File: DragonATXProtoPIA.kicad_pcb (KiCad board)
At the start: 2 copper layers, 168.7 x 104.9 mm, 78 parts, among them IC1 MC6821, IC10 MT8816, IC11 74LS138, IC12 W65C51, IC13 MAX232, IC14 M48Tx2, IC15 74LS21, IC2 MC6821, IC3 74LS138, IC4 4050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

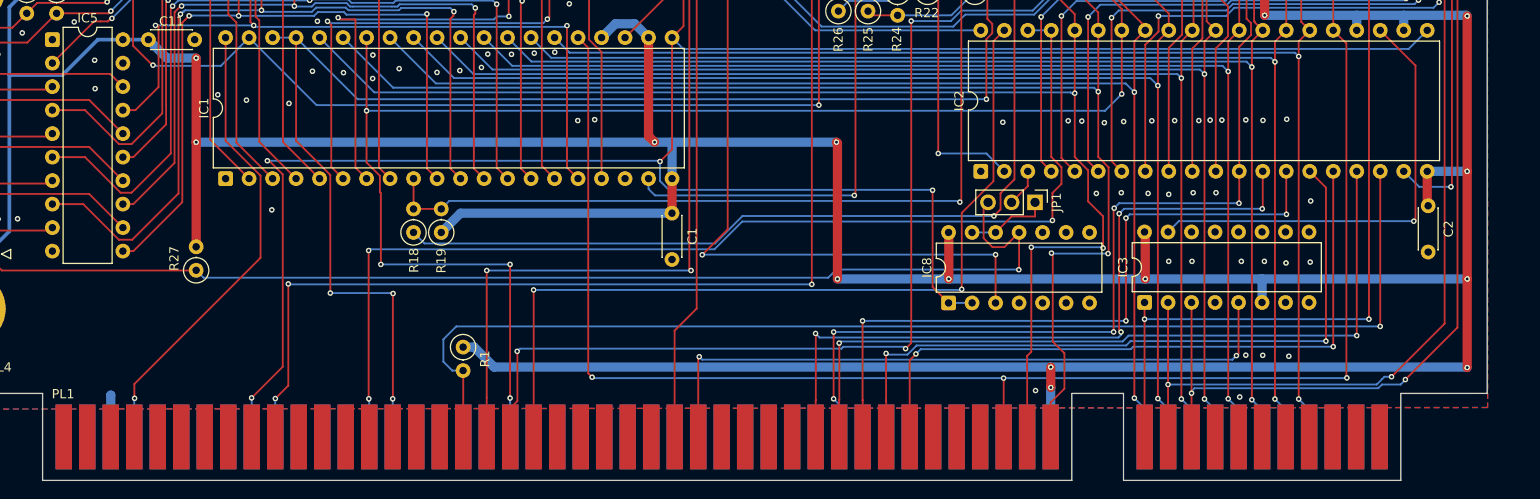
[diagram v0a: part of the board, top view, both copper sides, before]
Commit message: upgrade card edge spec
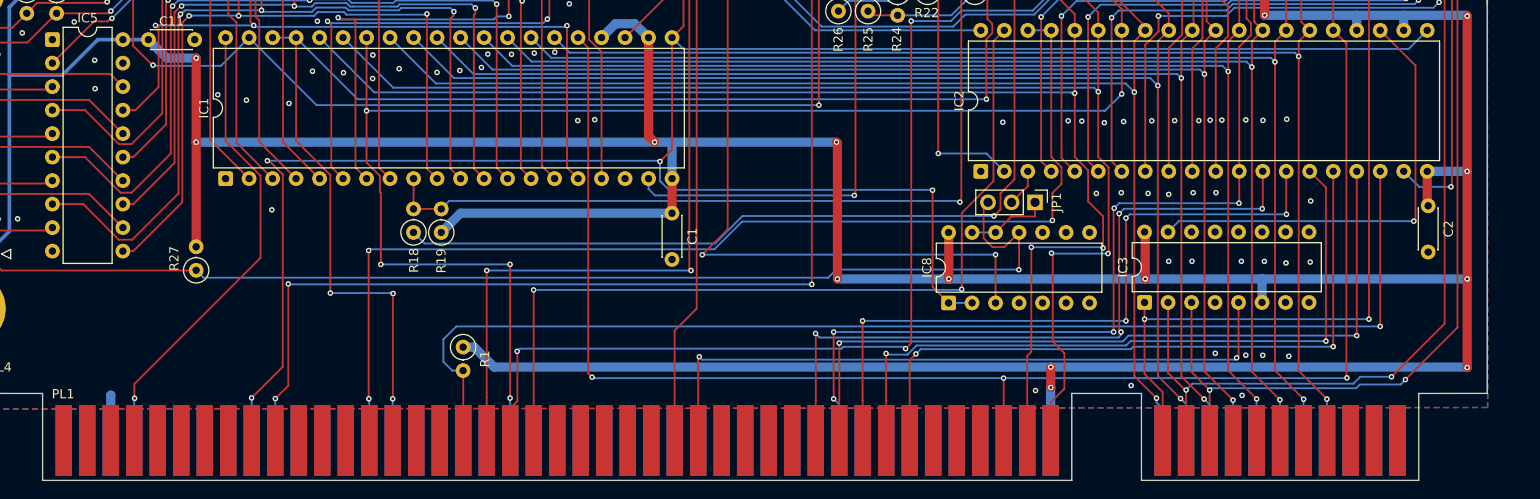
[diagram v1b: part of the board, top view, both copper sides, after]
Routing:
- net /A4: track 128.2 -> 126.7 mm
- net /A3: track 206.6 -> 205.8 mm
- net /D4: track 227.2 -> 228.0 mm
- net /D6: track 241.2 -> 242.0 mm
- net /A2: track 184.5 -> 185.3 mm
- net /D0: track 225.5 -> 226.3 mm
- net /D5: track 234.2 -> 235.0 mm
- net /D3: track 224.8 -> 225.6 mm
- net /D2: track 219.1 -> 219.9 mm
- net /D1: track 221.5 -> 222.3 mm
- net /D7: track 245.8 -> 246.6 mm
- net GND: vias 89 -> 91
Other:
- outline, holes or cut-outs redrawn

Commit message: prepare for fabrication
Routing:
- net /A2: track 185.3 -> 184.6 mm, vias 5 -> 3
- net GND: vias 91 -> 100

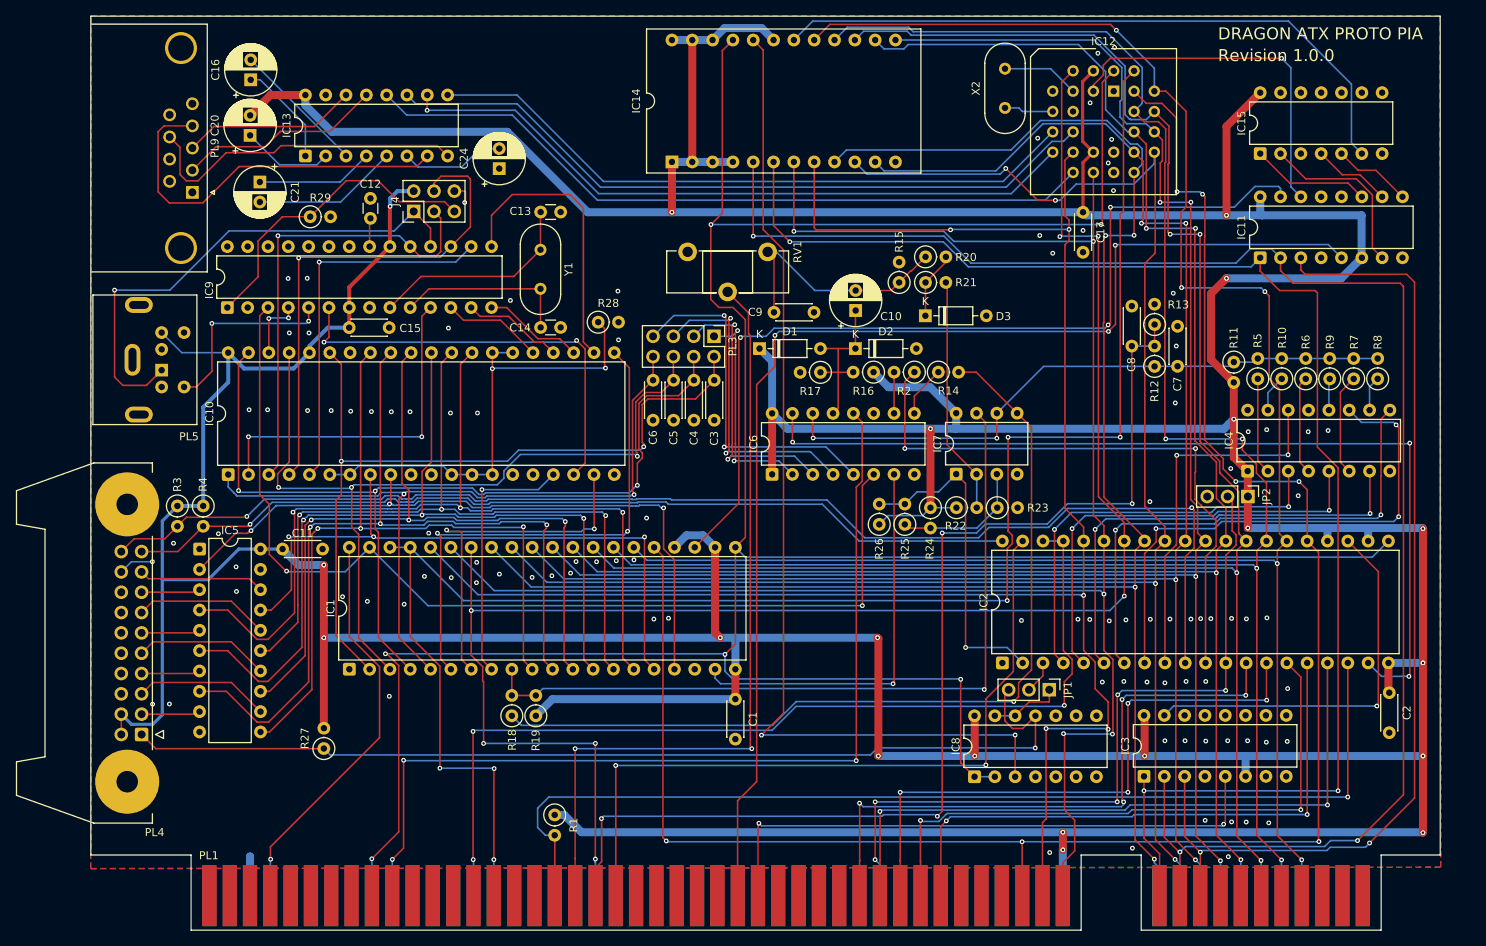
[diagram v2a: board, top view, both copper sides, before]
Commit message: Rectify slot edge and vertical dimensions
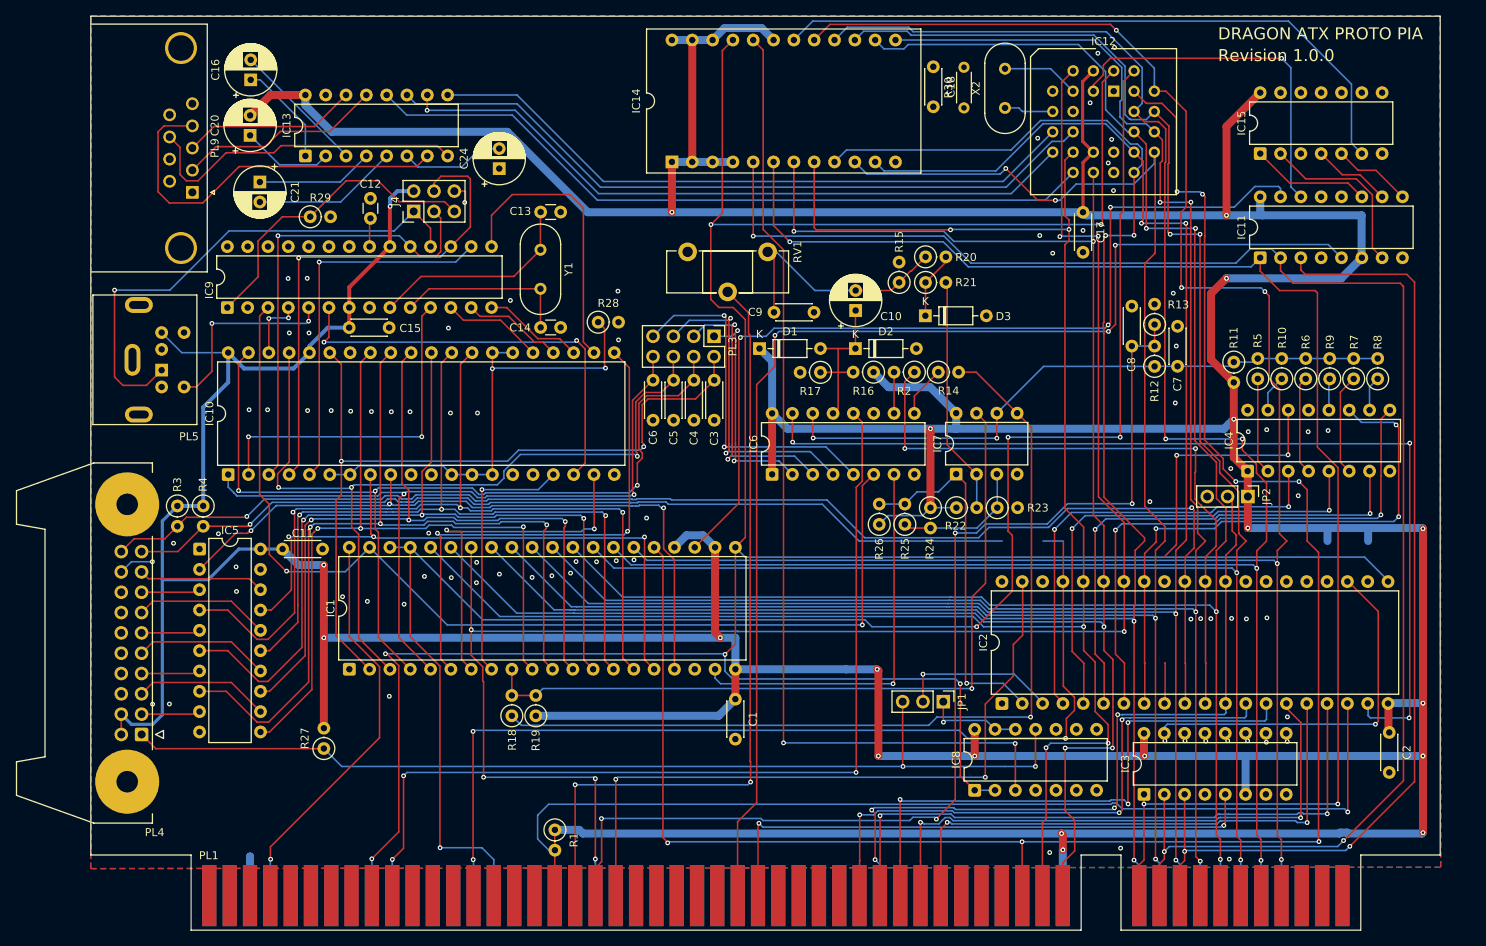
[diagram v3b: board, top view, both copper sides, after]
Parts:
- added C18: 30pF, Capacitor_THT:C_Disc_D4.3mm_W1.9mm_P5.00mm, F.Cu at (133.6, 20.7)
- added R30: 1M, Resistor_THT:R_Axial_DIN0204_L3.6mm_D1.6mm_P5.08mm_Horizontal, F.Cu at (137.5, 25.8)
- moved JP1 13.3 mm to (134.9, 100.0)
- moved IC2 5.07 mm to (142.2, 100.3)
- moved C2 4.97 mm to (190.6, 103.9)
- moved IC3 2.25 mm to (160.0, 111.6)
- moved R1 1.87 mm to (86.3, 116.1)
- moved IC8 1.69 mm to (138.8, 111.1)
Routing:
- net Net-(IC2-PA1): track 4.08 -> 20.0 mm, vias 0 -> 1
- net /PIADAC5: track 46.1 -> 37.8 mm
- net +5V: track 952.4 -> 945.9 mm
- net /CB2: track 115.9 -> 122.1 mm
- net /CSS: track 77.8 -> 72.0 mm, vias 4 -> 3
- net /MOTOR: track 92.5 -> 87.3 mm
- net /PIADAC2: track 57.1 -> 62.1 mm
- net /PIADAC4: track 66.6 -> 71.6 mm
- net /PIADAC0: track 51.5 -> 56.5 mm
- net /PIADAC1: track 54.8 -> 59.8 mm
- net Net-(IC2-PB1): track 74.9 -> 79.9 mm
- net /PIADAC3: track 64.6 -> 69.6 mm
- net /P.BUSY: track 161.2 -> 166.2 mm
- net /PC0: track 41.6 -> 46.3 mm
- net /~{A}/G: track 84.6 -> 80.3 mm
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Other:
- outline, holes or cut-outs redrawn

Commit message: shrink board
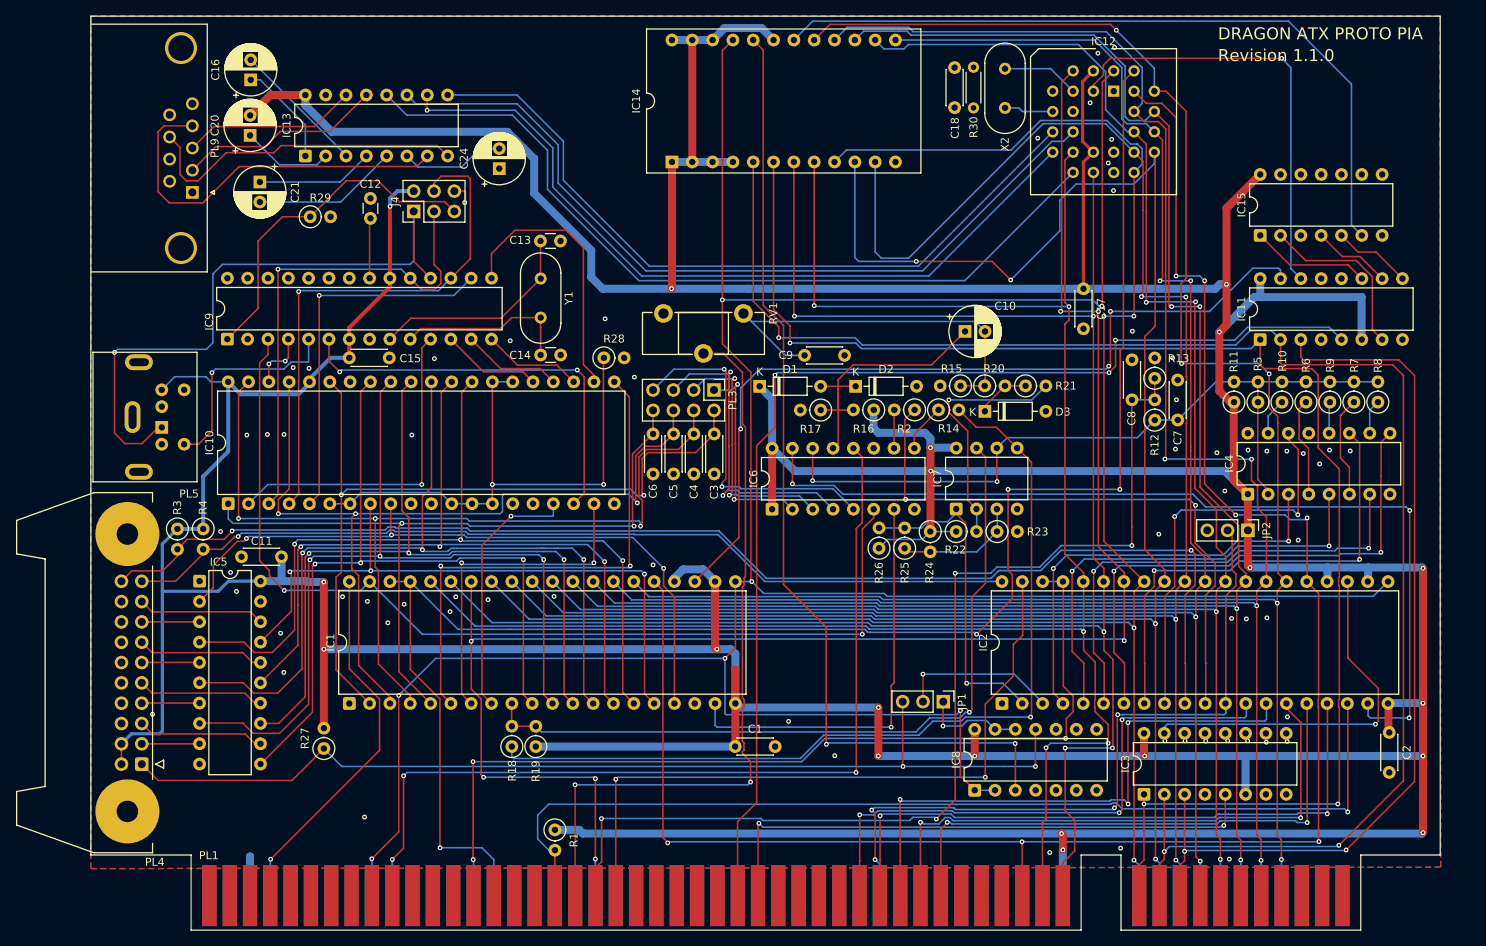
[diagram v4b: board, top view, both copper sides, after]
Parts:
- moved R21 18.0 mm to (145.2, 60.6)
- moved R20 17.7 mm to (140.1, 60.6)
- moved R15 15.0 mm to (137.0, 60.6), turned to 180 degrees
- moved D3 14.1 mm to (140.1, 63.7)
- moved C10 13.9 mm to (137.6, 53.7), turned to 0 degrees
- moved IC11 10.2 mm to (174.5, 54.8)
- moved IC15 10.2 mm to (174.5, 41.7)
- moved C17 9.57 mm to (152.4, 48.4)
- moved RV1 8.27 mm to (109.9, 51.5)
- moved PL5 7.16 mm to (37.2, 65.7)
- moved C7 6.72 mm to (164.2, 64.8)
- moved R12 6.72 mm to (161.3, 64.8)
- moved C8 6.72 mm to (158.5, 62.3)
- moved R13 6.72 mm to (161.3, 59.6)
- moved C3 6.71 mm to (106.2, 71.6)
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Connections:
- R11 pad 1: Net-(IC6-Y0) -> +5V
- R11 pad 2: +5V -> Net-(IC6-Y0)
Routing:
- net Net-(C10-Pad2): track 31.4 -> 50.8 mm
- net Net-(D1-A): track 21.6 -> 38.6 mm
- net /D1: track 222.7 -> 238.1 mm
- net /PS2.DATA: track 64.7 -> 79.9 mm
- net /D2: track 220.5 -> 234.6 mm
- net +5V: track 945.9 -> 959.6 mm
- net /PIADAC5: track 37.8 -> 50.5 mm
- net /PIADAC4: track 71.6 -> 59.8 mm, vias 3 -> 2
- net /~{CTS}: track 82.7 -> 94.3 mm
- net /TxD: track 90.9 -> 102.4 mm
- net /~{DTR}: track 86.6 -> 98.0 mm
- net /RxD: track 92.7 -> 103.9 mm
- net /P0: track 154.0 -> 142.9 mm
- net /A4: track 124.6 -> 113.9 mm
- net /P0b: track 44.7 -> 54.9 mm
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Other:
- board text added: "Revision 1.1.0"
- board text removed: "Revision 1.0.0"

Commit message: shrink dimensions
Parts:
- moved C16 39.6 mm to (87.6, 27.6), turned to -90 degrees
- moved C20 13.6 mm to (58.4, 38.2)
- moved IC14 10.2 mm to (101.0, 42.8)
- moved PL9 9.18 mm to (41.0, 45.5)
- moved IC13 8.96 mm to (63.7, 34.6)
- moved C24 8.48 mm to (79.6, 41.9)
- moved R30 7.98 mm to (138.7, 33.8)
- moved IC12 7.98 mm to (156.2, 31.7)
- moved X2 7.98 mm to (142.6, 28.9)
- moved C18 7.91 mm to (136.2, 28.7)
- moved C21 6.33 mm to (47.4, 41.1)
- moved J4 4.56 mm to (68.7, 43.3)
- moved R29 4.40 mm to (55.7, 43.8)
- moved C12 4.20 mm to (63.2, 43.8), turned to 180 degrees
- moved IC15 0.85 mm to (174.5, 42.6)
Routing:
- net /xTxD: track 22.0 -> 55.3 mm
- net +5V: track 959.6 -> 927.8 mm
- net /xRxD: track 25.6 -> 49.1 mm
- net /R/W: track 359.8 -> 341.6 mm
- net /A1: track 239.4 -> 221.2 mm
- net /A0: track 237.7 -> 219.6 mm
- net /D2: track 234.6 -> 216.6 mm
- net Net-(IC13-C1+): track 13.0 -> 26.8 mm, vias 0 -> 1
- net Net-(IC13-C2+): track 14.7 -> 28.1 mm
- net Net-(IC13-C2-): track 18.2 -> 31.3 mm
- net /D1: track 238.1 -> 225.1 mm
- net /RxD: track 103.9 -> 92.3 mm
- net /~{CTS}: track 94.3 -> 83.6 mm
- net /P0b: track 54.9 -> 44.5 mm
- net /TxD: track 102.4 -> 91.9 mm
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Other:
- board size 168.7 x 104.9 mm -> 168.7 x 97.2 mm
